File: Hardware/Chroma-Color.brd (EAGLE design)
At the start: 103.9 x 48 mm, 65 parts, among them J1 15-91-1102, J2 87832-6422, J3 1775470-6, J4 D2514-6V0C-AR-WD, J7 26-64-4040, U1 EP4CE6E22C8N, U2 ADP3338AKCZ-3.3-RL, U3 ADP3338AKCZ-2.5-RL, U4 NCV565ST12T3G, U5 M25P40-VMN6TPBCT, X1 ASDMB-50.000MHZ-LC-T

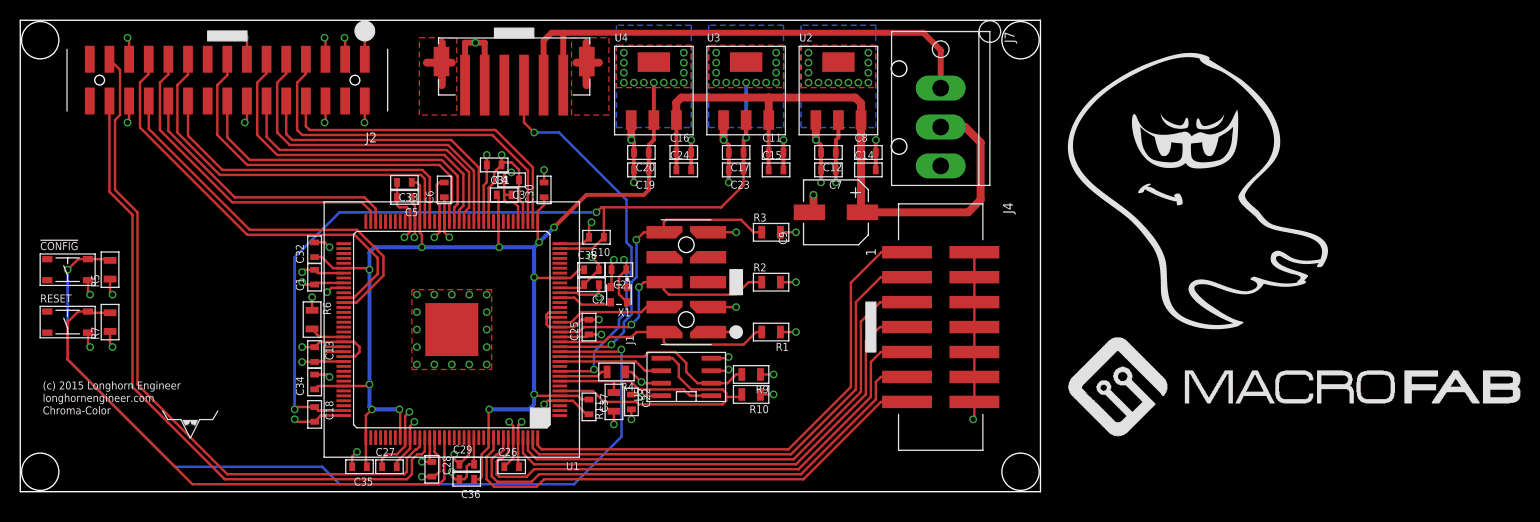
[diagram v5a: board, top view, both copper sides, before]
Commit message: Silkscreen done. Added 2SW and 2LED.
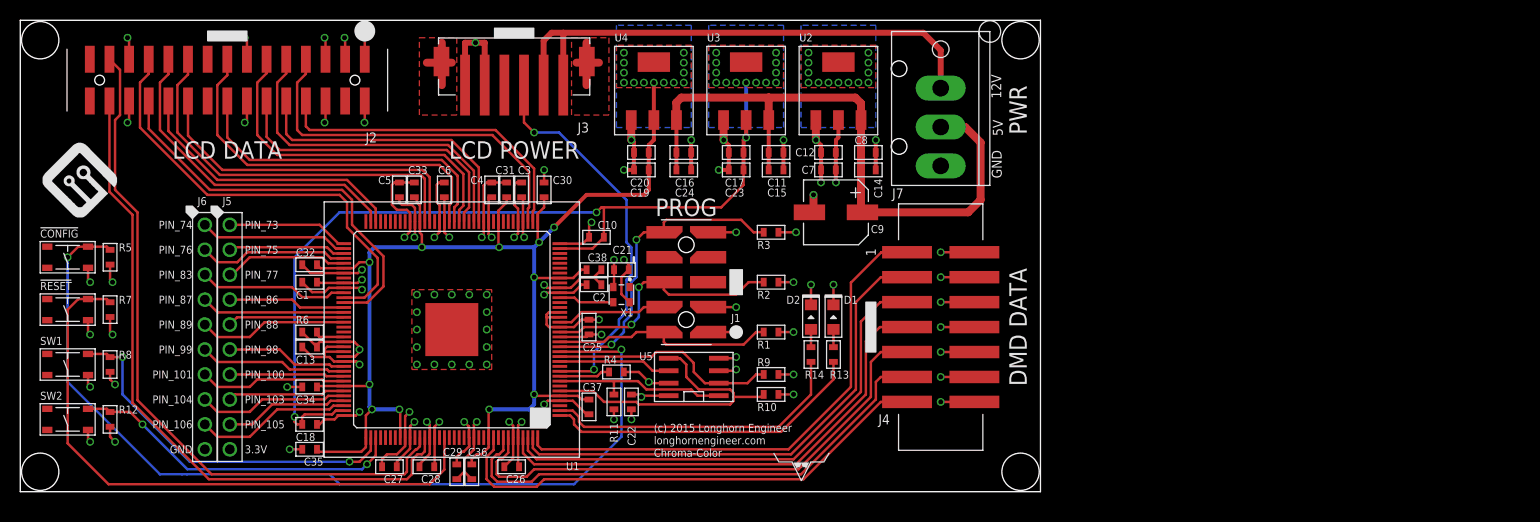
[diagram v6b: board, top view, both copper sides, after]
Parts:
- removed LOGO1: SPOOKY_LOGOSPOOKY_LOGO, PP_Aesthetics:SPOOKY_LOGO
- removed RESET: (no value), MF_Switches:TACT4.2MM
- added !RESET, SW1, SW2: (no value), MF_Switches:TACT4.2MM
- added D1, D2: (no value), MF_LEDs:LED0805
- added J5, J6: (no value), MF_Connectors:PTH_2.54MM_01X10
- added R12, R8: 10K, MF_Passives:R0603
- added R13, R14: 330, MF_Passives:R0603
- R1, R10, R11, R2, R3, R4, R5, R6, R7, R9: device MF_Passives:R0805 -> MF_Passives:R0603
- U$2: value MF_LOGOLOGO_TEXT -> MF_LOGOLOGO_MEDIUM; device PP_Aesthetics:MF_LOGO_TEXT -> PP_Aesthetics:MF_LOGO_MEDIUM
- moved U$2 107.0 mm to (2.29, 27.9)
- moved U$1 62.4 mm to (64.5, 1.02)
- moved U$3 62.4 mm to (81.5, 1.02)
- moved C35 5.38 mm to (29.5, 4.32)
- moved C4 2.55 mm to (48.0, 30.7), turned to 90 degrees
- moved R10 2.03 mm to (76.5, 9.91)
- moved R9 2.03 mm to (76.5, 11.9)
- moved C32 1.61 mm to (29.5, 23.1), turned to 180 degrees
- moved C3 1.44 mm to (51.1, 30.7), turned to 90 degrees
- moved R6 1.30 mm to (29.5, 16.3), turned to 0 degrees
- moved R7 1.27 mm to (9.14, 18.5)
- moved !CONFIG 1.27 mm to (4.83, 23.9)
- moved R5 1.27 mm to (9.14, 23.9)
- moved C29 1.27 mm to (44.5, 2.03), turned to 270 degrees
- moved C33 1.27 mm to (40.1, 30.7), turned to 90 degrees
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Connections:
- new net N$1: D1.ANODE, R13.P$2
- new net N$2: D2.ANODE, R14.P$2
- net 3.3V: now also J5.P$10, R12.P$1, R8.P$1
- net GND: now also !RESET.P$4, D1.CATHODE, D2.CATHODE, J6.P$10, SW1.P$4, SW2.P$4; no longer RESET.P$4
- net PIN_1: now also R13.P$1
- net PIN_100: now also J5.P$7
- net PIN_101: now also J6.P$7
- net PIN_103: now also J5.P$8
- net PIN_104: now also J6.P$8
- net PIN_105: now also J5.P$9
- net PIN_106: now also J6.P$9
- net PIN_110: now also R8.P$2, SW1.P$2
- net PIN_111: now also R12.P$2, SW2.P$2
- net PIN_2: now also R14.P$1
- net PIN_73: now also J5.P$1
- net PIN_74: now also J6.P$1
- net PIN_75: now also J5.P$2
- net PIN_76: now also J6.P$2
- net PIN_77: now also J5.P$3
- net PIN_83: now also J6.P$3
- net PIN_86: now also J5.P$4
- net PIN_87: now also J6.P$4
- net PIN_88: now also J5.P$5
- net PIN_89: now also J6.P$5
- net PIN_98: now also J5.P$6
- net PIN_99: now also J6.P$6
- net RESET: now also !RESET.P$2; no longer RESET.P$2
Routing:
- net PIN_110: track 0.00 -> 37.4 mm, vias 0 -> 2
- net PIN_111: track 0.00 -> 34.3 mm, vias 0 -> 2
- net PIN_1: track 0.00 -> 32.8 mm
- net PIN_2: track 0.00 -> 31.2 mm
- net GND: track 213.1 -> 238.8 mm, vias 62 -> 71
- net PIN_106: track 0.00 -> 16.0 mm
- net PIN_76: track 0.00 -> 15.4 mm
- net PIN_104: track 0.00 -> 15.3 mm
- net PIN_89: track 0.00 -> 15.3 mm
- net PIN_83: track 0.00 -> 15.3 mm
- net PIN_74: track 0.00 -> 15.1 mm
- net PIN_99: track 0.00 -> 15.1 mm
- net PIN_101: track 0.00 -> 15.1 mm
- net PIN_87: track 0.00 -> 14.7 mm
- net PIN_105: track 0.00 -> 12.6 mm
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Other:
- board text added: "DMD DATA"
- board text added: "LCD DATA"
- board text added: "LCD POWER"
- board text added: "PROG"
- board text added: "PWR"

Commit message: Added 750ohm and 10K pulldowns on DMD con.
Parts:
- added R15, R16, R17, R18, R19, R20, R21: 750, MF_Passives:R0603
- added R22, R23, R24, R25, R26, R27, R28: 10K, MF_Passives:R0603
- moved U$2 77.9 mm to (75.4, 1.02)
- moved U$1 67.9 mm to (2.03, 27.7)
- moved U$3 60.0 mm to (28.4, 29.0)
- moved R13 17.8 mm to (67.1, 5.59), turned to 0 degrees
- moved D1 17.1 mm to (70.9, 5.59), turned to 180 degrees
- moved R14 14.9 mm to (67.1, 7.62), turned to 0 degrees
- moved D2 14.0 mm to (70.9, 7.62), turned to 180 degrees
- moved R1 1.27 mm to (75.2, 16.3)
- moved R10 1.27 mm to (75.2, 9.91)
- moved R2 1.27 mm to (75.2, 21.3)
- moved R3 1.27 mm to (75.2, 26.4)
- moved R9 1.27 mm to (75.2, 11.9)
- moved J4 1.02 mm to (94.7, 16.8)
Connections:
- new net N$3: J4.1, R15.P$2
- new net N$4: J4.3, R16.P$2
- new net N$5: J4.5, R17.P$2
- new net N$6: J4.7, R18.P$2
- new net N$7: J4.9, R19.P$2
- new net N$8: J4.11, R20.P$2
- new net N$9: J4.13, R21.P$2
- net CLOCK: now also R15.P$1, R22.P$1; no longer J4.1
- net DATA: now also R16.P$1, R23.P$1; no longer J4.3
- net ENABLE: now also R21.P$1, R28.P$1; no longer J4.13
- net GND: now also R22.P$2, R23.P$2, R24.P$2, R25.P$2, R26.P$2, R27.P$2, R28.P$2
- net LATCH: now also R17.P$1, R24.P$1; no longer J4.5
- net REG0: now also R20.P$1, R27.P$1; no longer J4.11
- net REG1: now also R19.P$1, R26.P$1; no longer J4.9
- net REG2: now also R18.P$1, R25.P$1; no longer J4.7
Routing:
- net GND: track 238.8 -> 273.3 mm, vias 71 -> 78
- net PIN_1: track 32.8 -> 12.6 mm
- net PIN_2: track 31.2 -> 12.8 mm
- net N$8: track 0.00 -> 5.60 mm
- net N$9: track 0.00 -> 4.97 mm
- net N$7: track 0.00 -> 4.97 mm
- net N$6: track 0.00 -> 4.97 mm
- net N$5: track 0.00 -> 4.97 mm
- net N$4: track 0.00 -> 4.97 mm
- net N$3: track 0.00 -> 4.97 mm
- net ENABLE: track 51.2 -> 48.3 mm
- net REG1: track 54.2 -> 51.4 mm
- net REG0: track 52.6 -> 50.2 mm
- net 3.3V: track 121.1 -> 119.0 mm
- net REG2: track 50.1 -> 48.2 mm
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
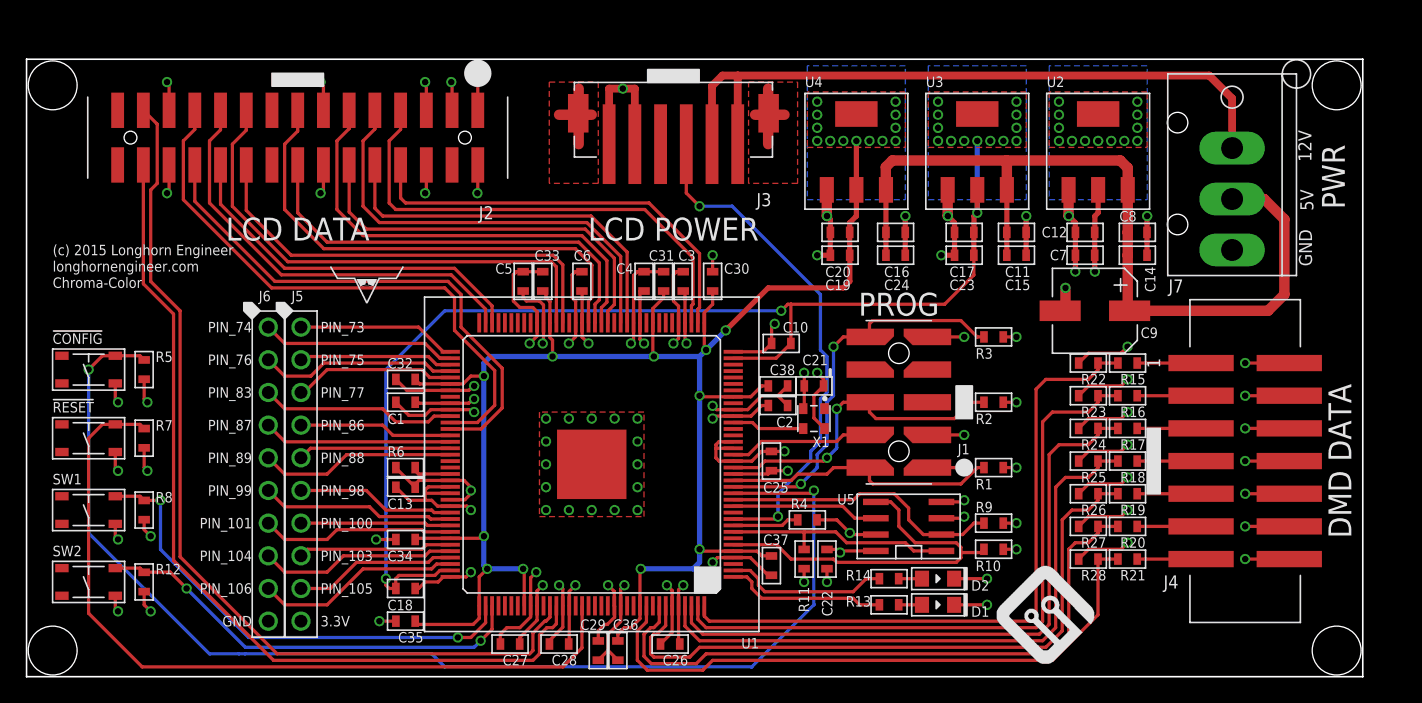
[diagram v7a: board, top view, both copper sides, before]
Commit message: Increased board area to add material around mount holes.
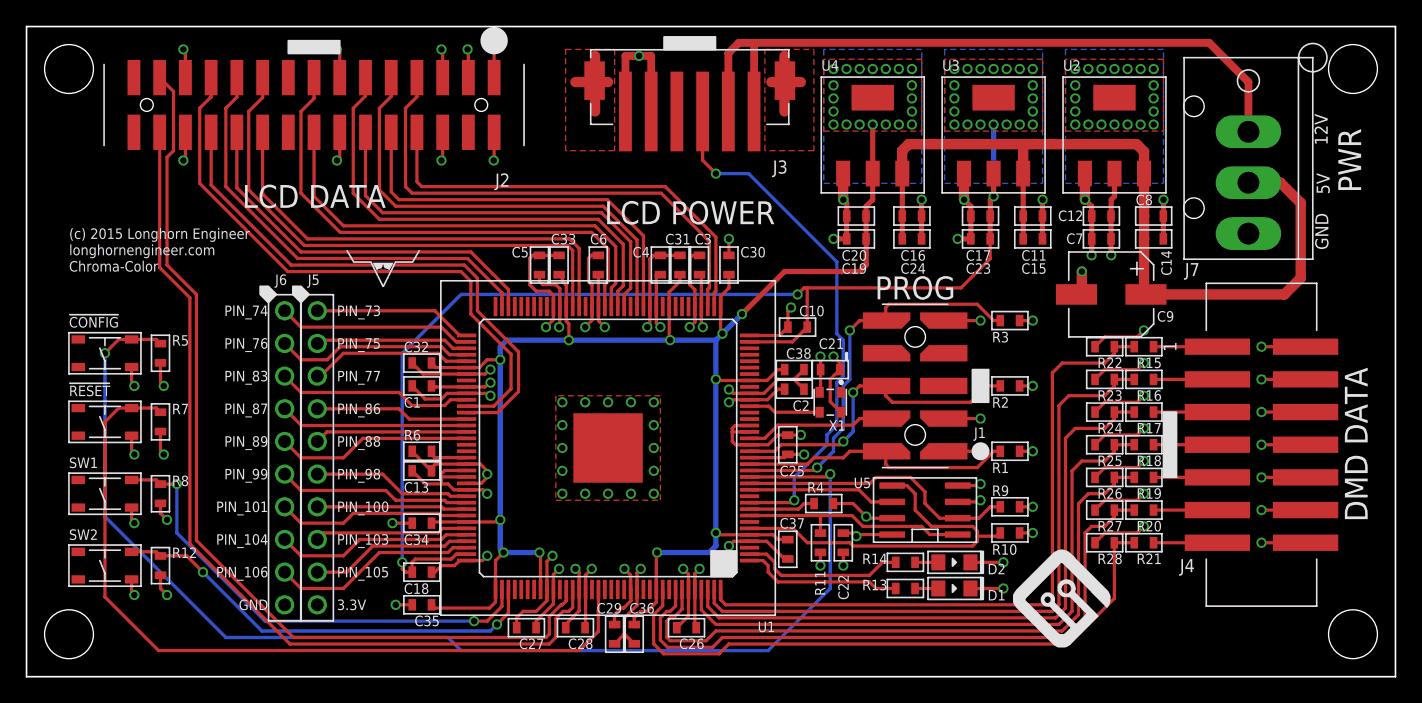
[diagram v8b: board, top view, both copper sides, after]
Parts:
- moved J2 2.84 mm to (22.4, 44.5)
- moved J3 2.84 mm to (51.6, 43.9)
- moved C16 1.80 mm to (68.8, 35.8)
- moved C17 1.80 mm to (74.2, 35.8)
- moved C23 1.80 mm to (74.2, 34.0)
- moved C24 1.80 mm to (68.8, 34.0)
- moved C1 1.80 mm to (30.7, 22.6)
- moved C19 1.80 mm to (64.5, 34.0)
- moved C20 1.80 mm to (64.5, 35.8)
- moved C34 1.80 mm to (30.7, 11.9)
- moved C37 1.80 mm to (59.2, 9.91)
- moved J5 1.80 mm to (22.6, 17.0)
- moved C18 1.80 mm to (30.7, 8.13)
- moved C35 1.80 mm to (30.7, 5.59)
- moved C26 1.80 mm to (51.3, 3.81)
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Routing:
- net ODDC-: track 38.4 -> 39.7 mm
- net ODD0+: track 33.0 -> 34.3 mm
- net EVEN2-: track 45.2 -> 46.5 mm
- net EVEN0-: track 39.4 -> 40.7 mm
- net ODD2+: track 31.0 -> 32.3 mm
- net ODD1-: track 34.7 -> 35.9 mm
- net ODD1+: track 29.9 -> 31.2 mm
- net ODD0-: track 38.1 -> 39.3 mm
- net EVEN2+: track 41.4 -> 42.7 mm
- net EVEN1-: track 33.5 -> 34.8 mm
- net EVEN1+: track 28.8 -> 30.0 mm
- net EVEN0+: track 34.4 -> 35.7 mm
- net PWM/EN: track 40.1 -> 41.4 mm
- net ODDC+: track 33.6 -> 34.9 mm
- net ODD2-: track 35.8 -> 37.0 mm
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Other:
- board size 103.9 x 48 mm -> 106.4 x 50.5 mm
